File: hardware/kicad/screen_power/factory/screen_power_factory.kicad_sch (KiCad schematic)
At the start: 12 parts, among them J1 AUX 5V INPUT, J2 SCREEN CONTROL, Q1 MMBT3904,215

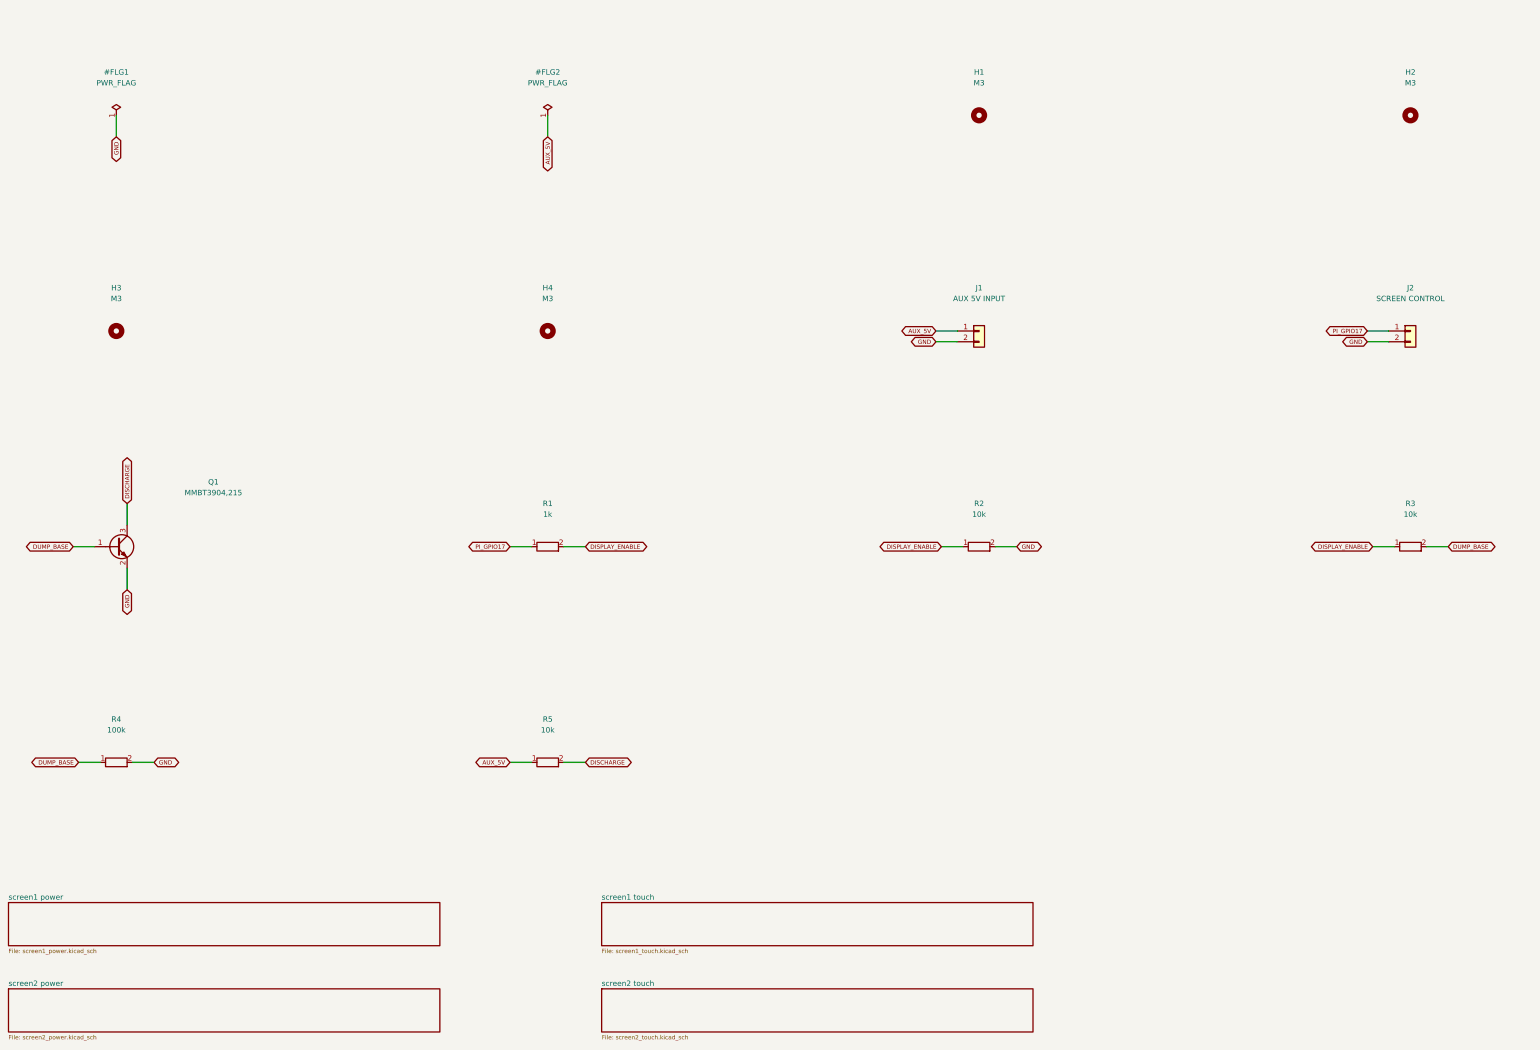
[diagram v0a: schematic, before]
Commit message: refactor(hardware): simplify and compact screen power boards
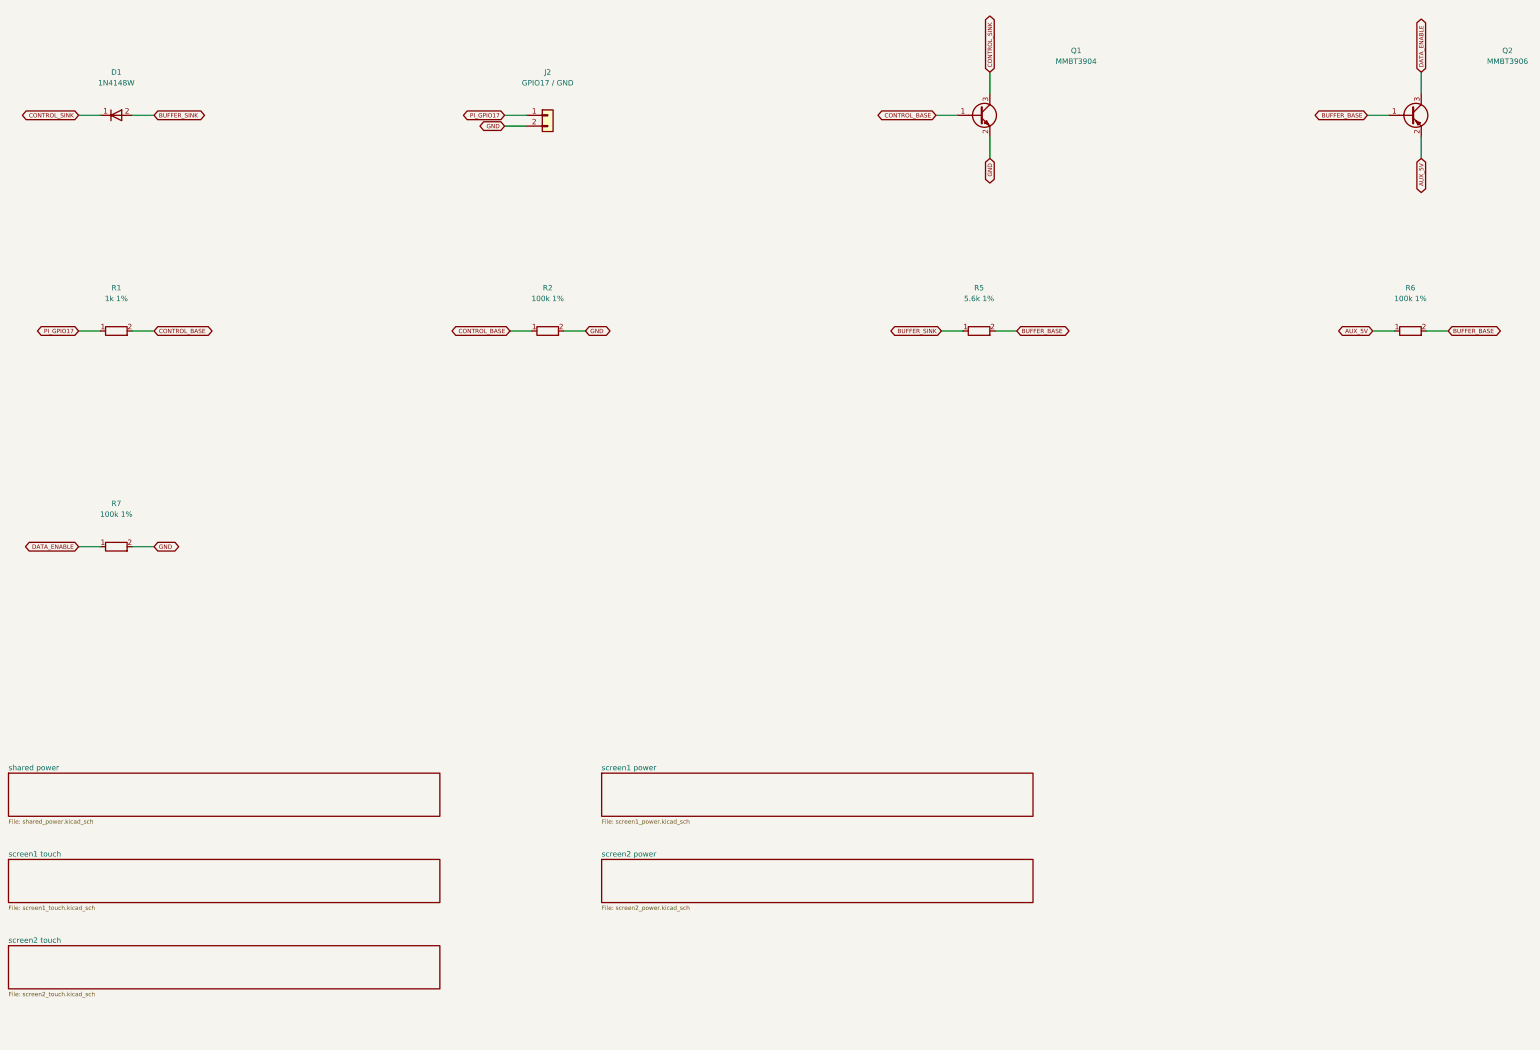
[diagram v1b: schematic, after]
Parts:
- removed H1, H2, H3, H4: M3, MountingHole:MountingHole_3.2mm_M3, symbol screen_symbols:Mechanical_MountingHole
- removed J1: AUX 5V INPUT, Connector_JST:JST_VH_B2P-VH_1x02_P3.96mm_Vertical, symbol screen_symbols:Connector_Generic_Conn_01x02
- removed R3: 10k, Resistor_SMD:R_0805_2012Metric, symbol screen_symbols:Device_R
- removed R4: 100k, Resistor_SMD:R_0805_2012Metric, symbol screen_symbols:Device_R
- added D1: 1N4148W, Diode_SMD:D_SOD-123, symbol screen_symbols:Diode_1N4148W
- added Q2: MMBT3906, Package_TO_SOT_SMD:SOT-23, symbol screen_symbols:Transistor_BJT_MMBT3906
- added R6, R7: 100k 1%, Resistor_SMD:R_0805_2012Metric, symbol screen_symbols:Device_R
- J2: value SCREEN CONTROL -> GPIO17 / GND
- Q1: value MMBT3904,215 -> MMBT3904
- R1: value 1k -> 1k 1%
- R2: value 10k -> 100k 1%; MPN RC0805FR-0710KL -> RC0805FR-07100KL
- R5: value 10k -> 5.6k 1%; MPN RC0805FR-0710KL -> RC0805FR-075K6L
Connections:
- net DUMP_BASE is gone; now on net CONTROL_BASE: Q1.1 (B)
- net AUX_5V: now also Q2.2 (E), R6.1; no longer R5.1
- net GND: now also R7.2
- net DISCHARGE renamed BUFFER_BASE
- net BUFFER_BASE: now also Q2.1 (B), R6.2; no longer Q1.3 (C)
- net DISPLAY_ENABLE renamed CONTROL_BASE
- new net BUFFER_SINK: D1.2 (A), R5.1
- new net CONTROL_SINK: D1.1 (K), Q1.3 (C)
- new net DATA_ENABLE: Q2.3 (C), R7.1
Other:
- added sheet shared power (shared_power.kicad_sch)
- moved on the sheet: J2, Q1, R1, R2, R5
